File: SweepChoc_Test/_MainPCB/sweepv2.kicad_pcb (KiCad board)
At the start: 2 copper layers, 216.9 x 86.9 mm, 59 parts, among them J1 AudioJack4dpb, J2 AudioJack4dpb, SW10 SW_Push, SW10_r1 SW_Push, SW11 SW_Push, SW11_r1 SW_Push, SW12 SW_Push, SW12_r1 SW_Push, SW14 SW_Push, SW14_r1 SW_Push, SW15 SW_Push, SW15_r1 SW_Push, SW16 SW_Push, SW16_r1 SW_Push, SW17 SW_Push, SW17_r1 SW_Push, SW18 SW_Push, SW18_r1 SW_Push, SW2 SW_Push, SW20 SW_Push, SW20_r1 SW_Push, SW21 SW_Push, SW21_r1 SW_Push, SW2_r1 SW_Push, SW3 SW_Push, SW3_r1 SW_Push, SW4 SW_Push, SW4_r1 SW_Push, SW5 SW_Push, SW5_r1 SW_Push, SW6 SW_Push, SW6_r1 SW_Push, SW8 SW_Push, SW8_r1 SW_Push, SW9 SW_Push, SW9_r1 SW_Push, U1 ProMicro-kbd, U2 ProMicro-kbd

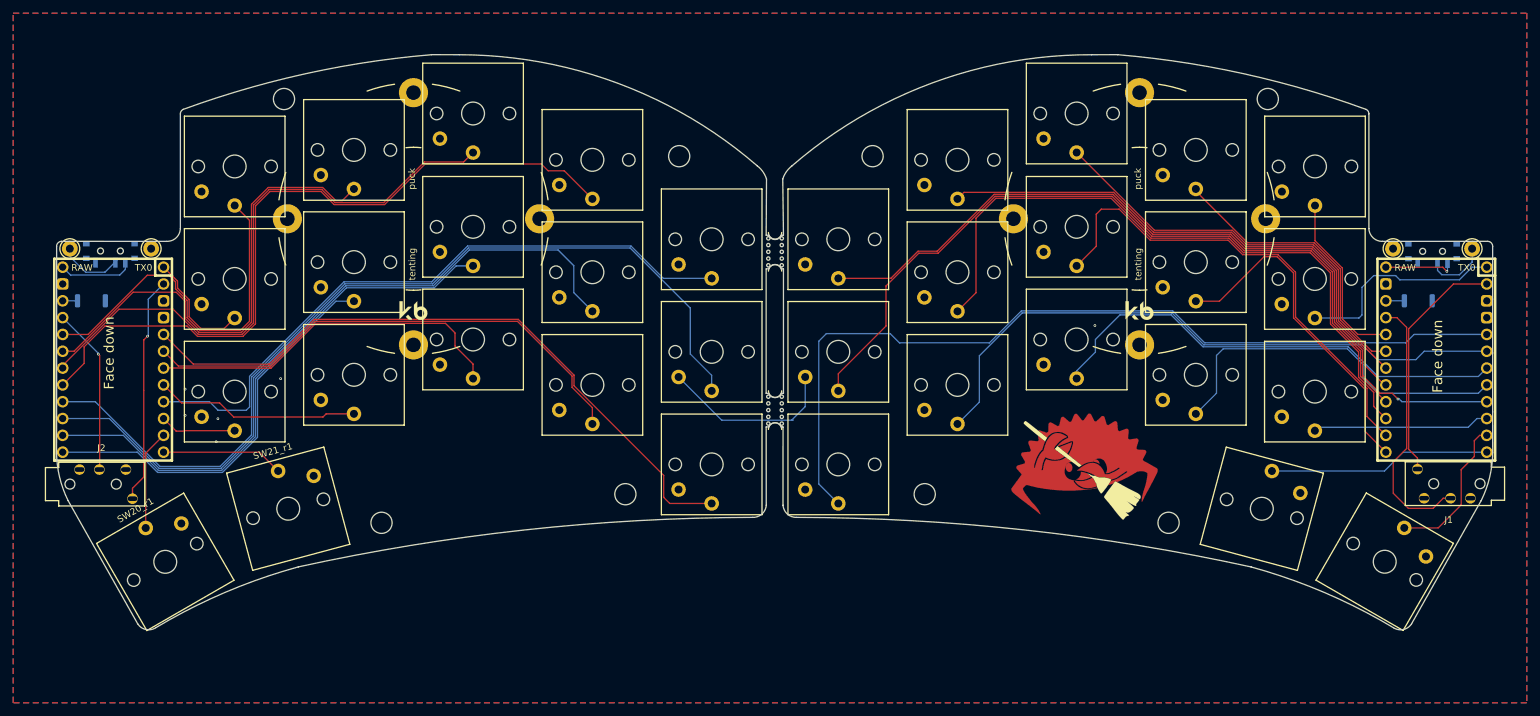
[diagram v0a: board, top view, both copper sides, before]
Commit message: routed all traces
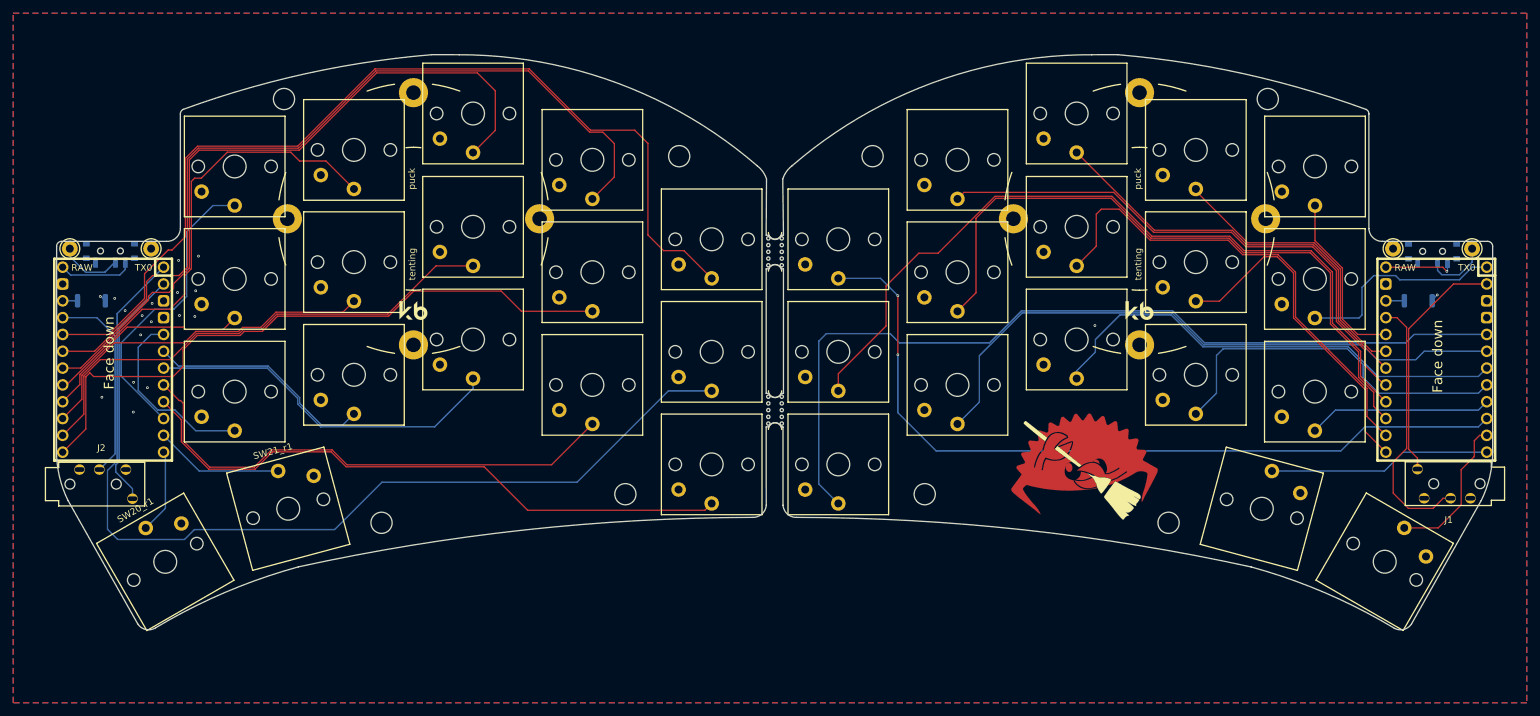
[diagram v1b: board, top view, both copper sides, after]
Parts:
- U1, U2: value ProMicro-kbd -> ProMicro
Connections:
- U1 pad 10: Switch15 -> Switch1
- U1 pad 9: Switch1 -> Switch15
- U2 pad 1: Switch10_r -> Switch6_r
- U2 pad 10: Switch15_r -> Switch5_r
- U2 pad 11: Switch16_r -> Switch17_r
- U2 pad 12: Switch17_r -> Switch16_r
- U2 pad 13: Switch9_r -> Switch7_r
- U2 pad 15: Switch7_r -> Switch9_r
- U2 pad 16: Switch6_r -> Switch10_r
- U2 pad 17: Switch2_r -> Switch4_r
- U2 pad 19: Switch4_r -> Switch2_r
- U2 pad 20: Switch5_r -> Switch1_r
- U2 pad 5: Switch11_r -> Switch15_r
- U2 pad 6: Switch12_r -> Switch14_r
- U2 pad 8: Switch14_r -> Switch12_r
- U2 pad 9: Switch1_r -> Switch11_r
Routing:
- net Switch1_r: track 98.3 -> 145.0 mm
- net gnd: track 27.4 -> 2.25 mm, vias 6 -> 19
- net Switch15_r: track 11.6 -> 28.2 mm
- net Switch2_r: track 110.9 -> 126.2 mm
- net Switch10_r: track 17.3 -> 32.4 mm
- net Switch3_r: track 90.9 -> 105.9 mm
- net Switch5_r: track 56.5 -> 45.6 mm
- net Switch7_r: track 108.1 -> 97.9 mm
- net Switch6_r: track 135.2 -> 144.3 mm
- net Switch11_r: track 101.8 -> 94.1 mm
- net Switch9_r: track 61.1 -> 53.5 mm
- net Switch8_r: track 82.1 -> 76.0 mm
- net vcc_r: track 25.3 -> 30.2 mm, vias 1 -> 0
- net Switch14_r: track 31.0 -> 34.5 mm
- net Switch4_r: track 72.8 -> 70.3 mm
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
